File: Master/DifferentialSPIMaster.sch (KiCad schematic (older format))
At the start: 27 parts

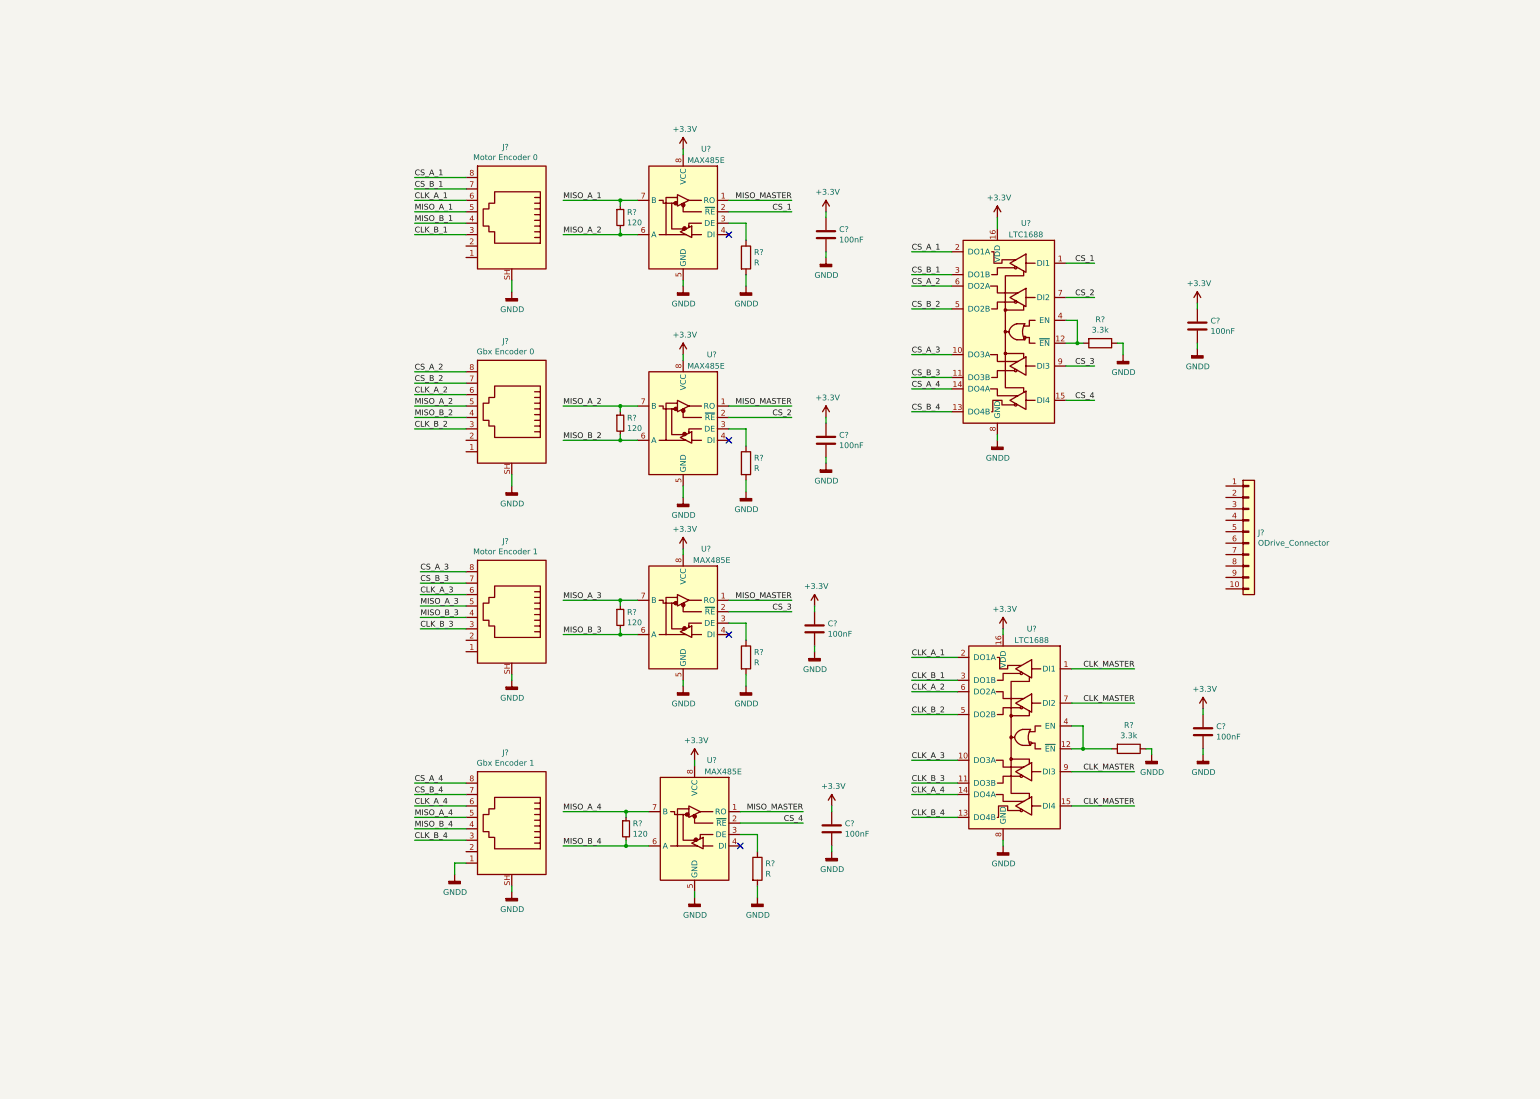
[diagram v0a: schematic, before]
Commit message: Add LPFs to single-ended signals
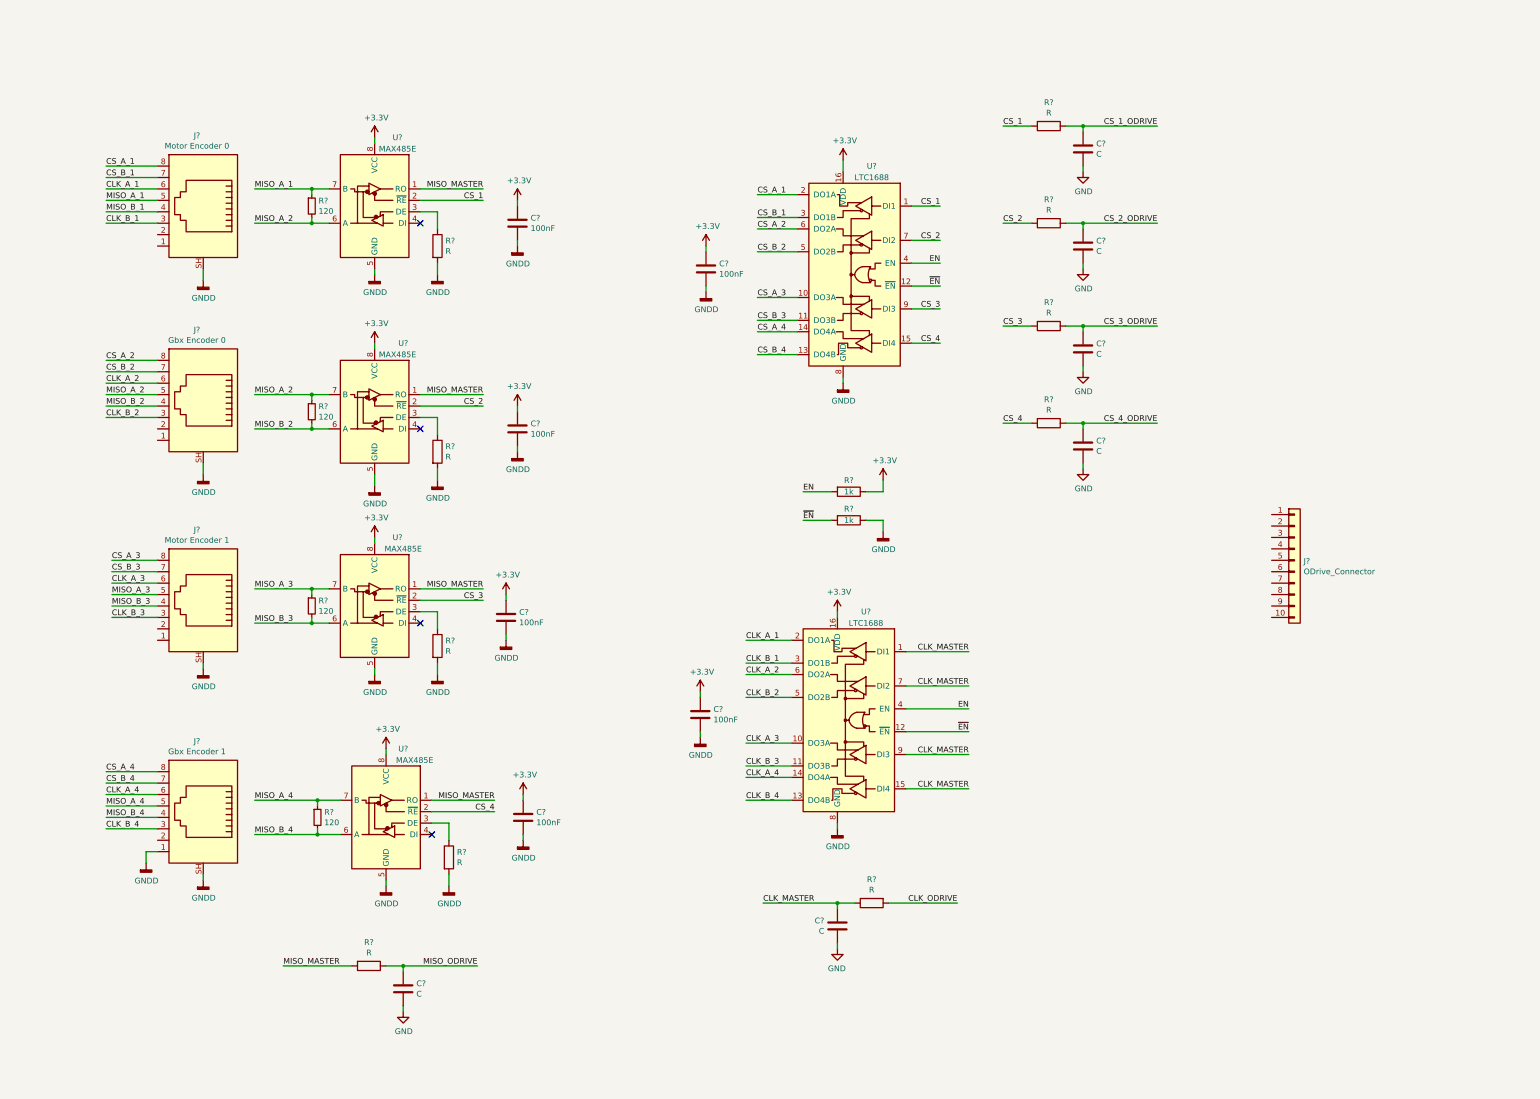
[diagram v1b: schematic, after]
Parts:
- removed R? (x2): 3.3k, symbol Device:R
- added C? (x6): C, symbol Device:C
- added R? (x6): R, symbol Device:R
- added R? (x2): 1k, symbol Device:R
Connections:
- net +3V3: now also R?.1
- net CLK_MASTER: now also C?.1, R?.1
- net CS_1: now also R?.2
- net CS_2: now also R?.2
- net CS_3: now also R?.2
- net CS_4: now also R?.2
- net GNDD: now also R?.1
- net MISO_MASTER: now also R?.2
- net EN: now reaches U?.4 (EN)
- net EN: now also U?.4 (EN), R?.2; no longer U?.12 (~EN)
- net ~EN: now reaches U?.12 (~EN)
- net ~EN: now also U?.12 (~EN), R?.2; no longer U?.4 (EN)
- new net CLK_ODRIVE: R?.2
- new net CS_1_ODRIVE: C?.1, R?.1
- new net CS_2_ODRIVE: C?.1, R?.1
- new net CS_3_ODRIVE: C?.1, R?.1
- new net CS_4_ODRIVE: C?.1, R?.1
- new net GND: C?.2, C?.2, C?.2, C?.2, C?.2, C?.2
- new net MISO_ODRIVE: C?.1, R?.1
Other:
- moved on the sheet: C?, J?, R?, U?

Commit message: Start laying out Master
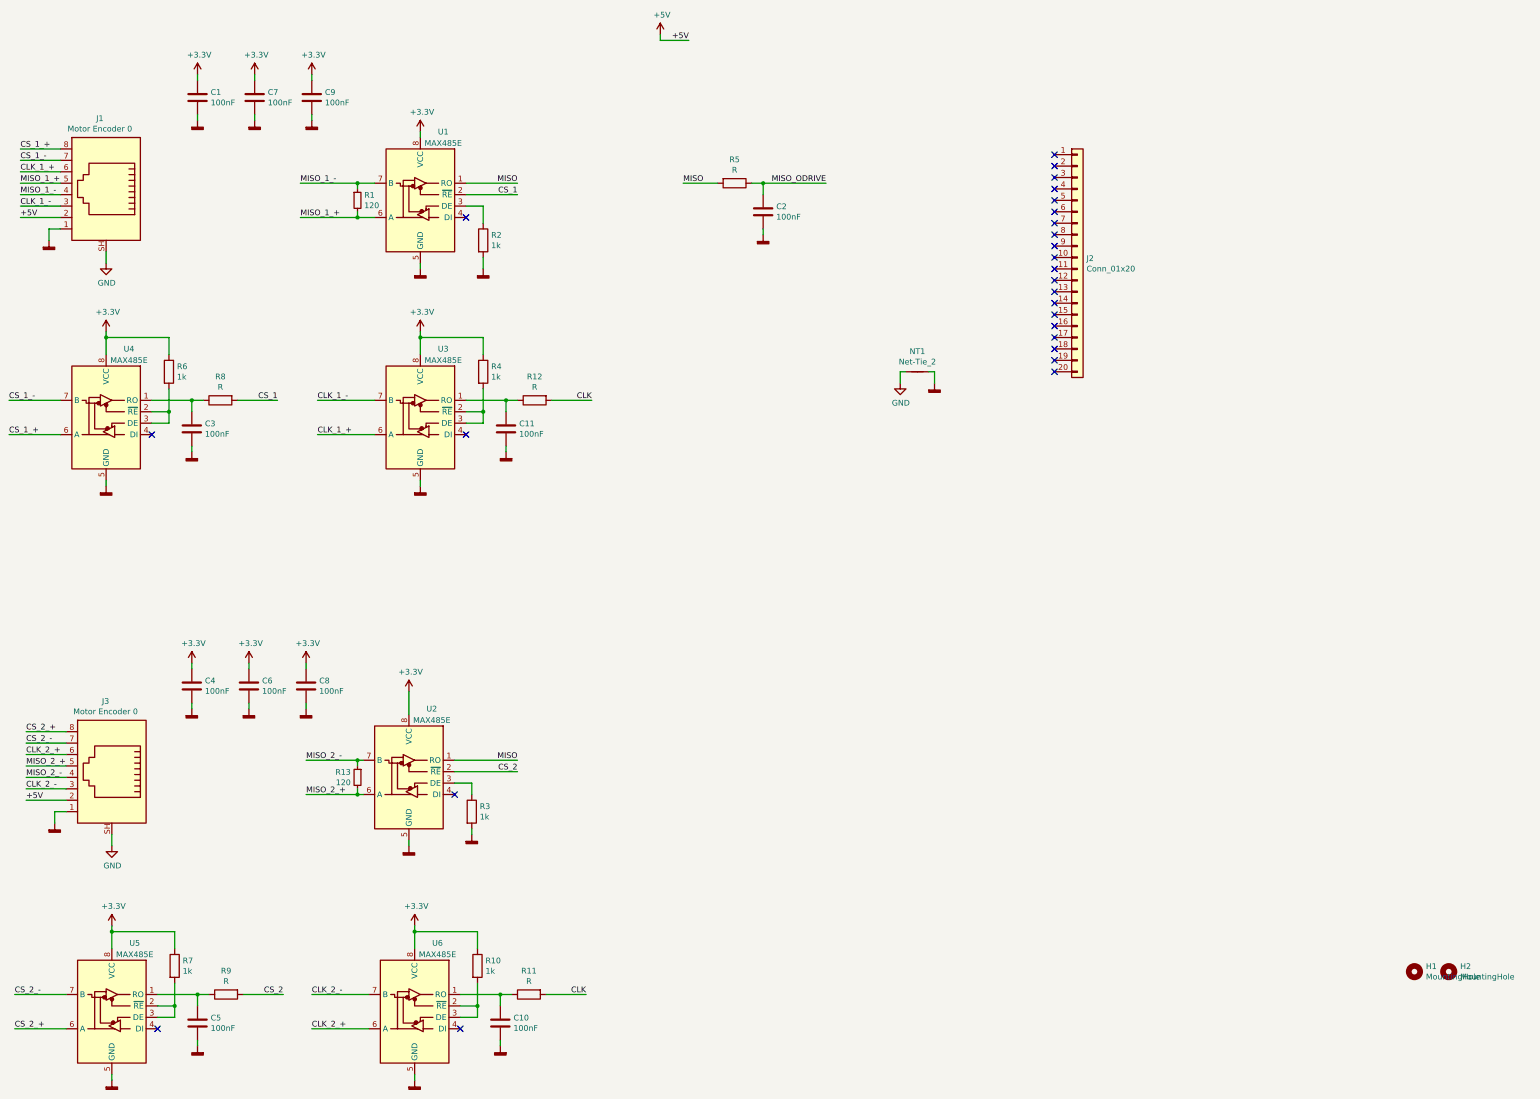
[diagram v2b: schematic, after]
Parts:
- removed C? (x5): 100nF, symbol Device:C
- removed C? (x6): C, symbol Device:C
- removed J?: Gbx Encoder 0, symbol Connector:8P8C_Shielded
- removed J?: Motor Encoder 1, symbol Connector:8P8C_Shielded
- removed J?: Gbx Encoder 1, symbol Connector:8P8C_Shielded
- removed J?: ODrive_Connector, symbol Connector_Generic:Conn_01x10
- removed R? (x9): R, symbol Device:R
- removed R? (x3): 120, symbol Device:R_Small
- removed R? (x2): 1k, symbol Device:R
- removed U? (x2): LTC1688, Package_SO:SOIC-16_3.9x9.9mm_P1.27mm, symbol Interface:LTC1688
- removed U? (x3): MAX485E, symbol Interface_UART:MAX485E
- added C10, C11, C2, C3, C4, C5, C6, C7, C8, C9: 100nF, Capacitor_SMD:C_0805_2012Metric_Pad1.15x1.40mm_HandSolder, symbol Device:C
- added H1, H2: MountingHole, MountingHole:MountingHole_3.5mm, symbol Mechanical:MountingHole
- added J2: Conn_01x20, Connector_PinHeader_2.54mm:PinHeader_1x20_P2.54mm_Vertical, symbol Connector_Generic:Conn_01x20
- added J3: Motor Encoder 0, Connector_RJ:RJ45_Amphenol_RJHSE5380, symbol Connector:8P8C_Shielded
- added NT1: Net-Tie_2, NetTie:NetTie-2_SMD_Pad0.5mm, symbol Device:Net-Tie_2
- added R10, R3, R4, R6, R7: 1k, Resistor_SMD:R_0805_2012Metric_Pad1.15x1.40mm_HandSolder, symbol Device:R
- added R11, R12, R5, R8, R9: R, Resistor_SMD:R_0805_2012Metric_Pad1.15x1.40mm_HandSolder, symbol Device:R
- added R13: 120, Resistor_SMD:R_0805_2012Metric_Pad1.15x1.40mm_HandSolder, symbol Device:R_Small
- added U2, U3, U4, U5, U6: MAX485E, Package_SO:SOIC-8_3.9x4.9mm_P1.27mm, symbol Interface_UART:MAX485E
- C1: renamed from C?; footprint (none) -> Capacitor_SMD:C_0805_2012Metric_Pad1.15x1.40mm_HandSolder
- J1: renamed from J?; footprint (none) -> Connector_RJ:RJ45_Amphenol_RJHSE5380
- R1: renamed from R?; footprint (none) -> Resistor_SMD:R_0805_2012Metric_Pad1.15x1.40mm_HandSolder
- R2: renamed from R?; value R -> 1k; footprint (none) -> Resistor_SMD:R_0805_2012Metric_Pad1.15x1.40mm_HandSolder
- U1: renamed from U?; footprint (none) -> Package_SO:SOIC-8_3.9x4.9mm_P1.27mm
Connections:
- net MISO_B_1 is gone; now on net MISO_1_-: J1.4
- net +3V3: now also C4.1, C6.1, C7.1, C8.1, C9.1, R10.1, R4.1, R6.1, R7.1, U2.8 (VCC), U3.8 (VCC), U4.8 (VCC), U5.8 (VCC), U6.8 (VCC)
- net CS_1: now also R8.2
- net CS_2: now also R9.2, U2.2 (~RE)
- net GND: now also J1.SH, J3.SH, NT1.1
- net GNDD: now also J1.1, C10.2, C11.2, C2.2, C3.2, C4.2, C5.2, C6.2, C7.2, C8.2, C9.2, J3.1, NT1.2, R3.2, U2.5 (GND), U3.5 (GND), U4.5 (GND), U5.5 (GND), U6.5 (GND); no longer J1.SH
- net MISO_ODRIVE: now also C2.1, R5.1
- net +5V: now reaches J1.2
- net +5V: now also J3.2
- net CLK_A_1 renamed CLK_1_+
- net CLK_1_+: now also U3.6 (A)
- net CLK_B_1 renamed CLK_1_-
- net CLK_1_-: now also U3.7 (B)
- net CS_A_1 renamed CS_1_+
- net CS_1_+: now also U4.6 (A)
- net CS_B_1 renamed CS_1_-
- net CS_1_-: now also U4.7 (B)
- net MISO_A_1 renamed MISO_1_-
- net MISO_1_-: no longer J1.5
- net MISO_A_2 renamed MISO_1_+
- net MISO_1_+: now also J1.5
- net MISO_MASTER renamed MISO
- net MISO: now also R5.2, U2.1 (RO)
- new net: R3.1, U2.3 (DE)
- new net: C3.1, R8.1, U4.1 (RO)
- new net: R6.2, U4.2 (~RE), U4.3 (DE)
- new net: C11.1, R12.1, U3.1 (RO)
- new net: R4.2, U3.2 (~RE), U3.3 (DE)
- new net: C10.1, R11.1, U6.1 (RO)
- new net: R10.2, U6.2 (~RE), U6.3 (DE)
- new net: C5.1, R9.1, U5.1 (RO)
- new net: R7.2, U5.2 (~RE), U5.3 (DE)
- new net CLK: R11.2, R12.2
- new net CLK_2_+: J3.6, U6.6 (A)
- new net CLK_2_-: J3.3, U6.7 (B)
- new net CS_2_+: J3.8, U5.6 (A)
- new net CS_2_-: J3.7, U5.7 (B)
- new net MISO_2_+: J3.5, R13.2, U2.6 (A)
- new net MISO_2_-: J3.4, R13.1, U2.7 (B)
- no-connect marks 4 -> 26
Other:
- moved on the sheet: C1, J1, R1, R2, U1
